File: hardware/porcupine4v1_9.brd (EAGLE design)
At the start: 24.4 x 27.4 mm, 33 parts, among them X1 PROGCON

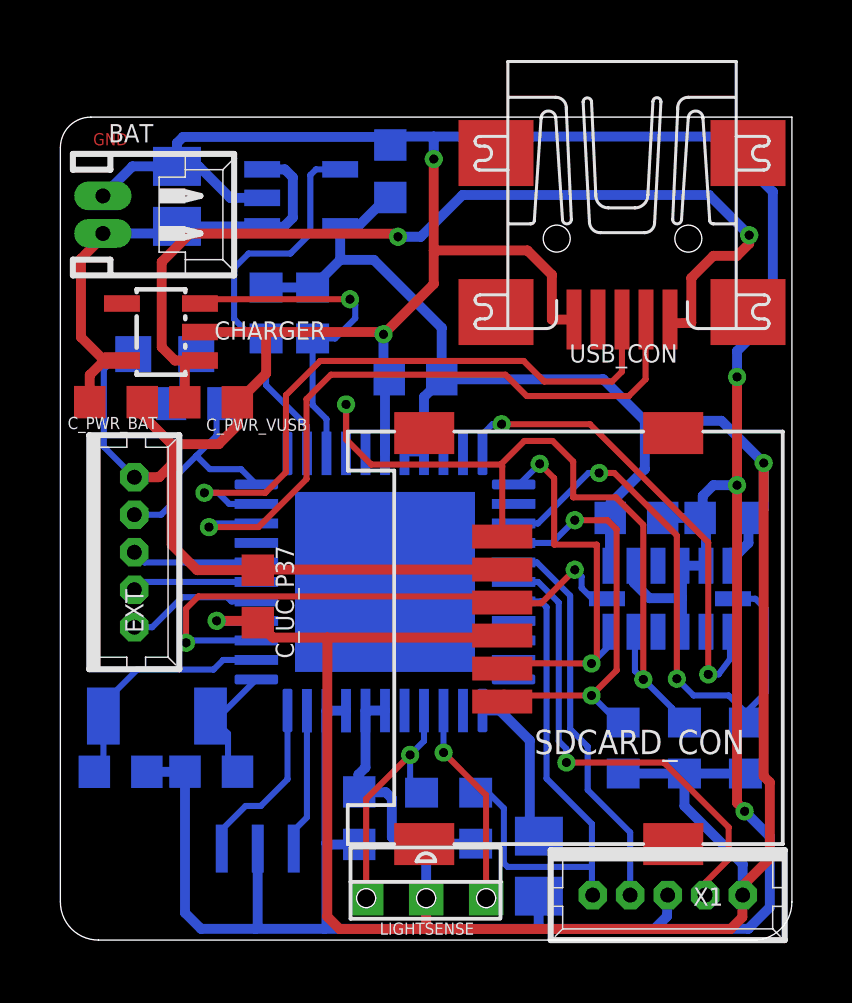
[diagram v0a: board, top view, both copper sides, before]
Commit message: updated porcupine4v1_9 for better placement of components; removed PWRGD
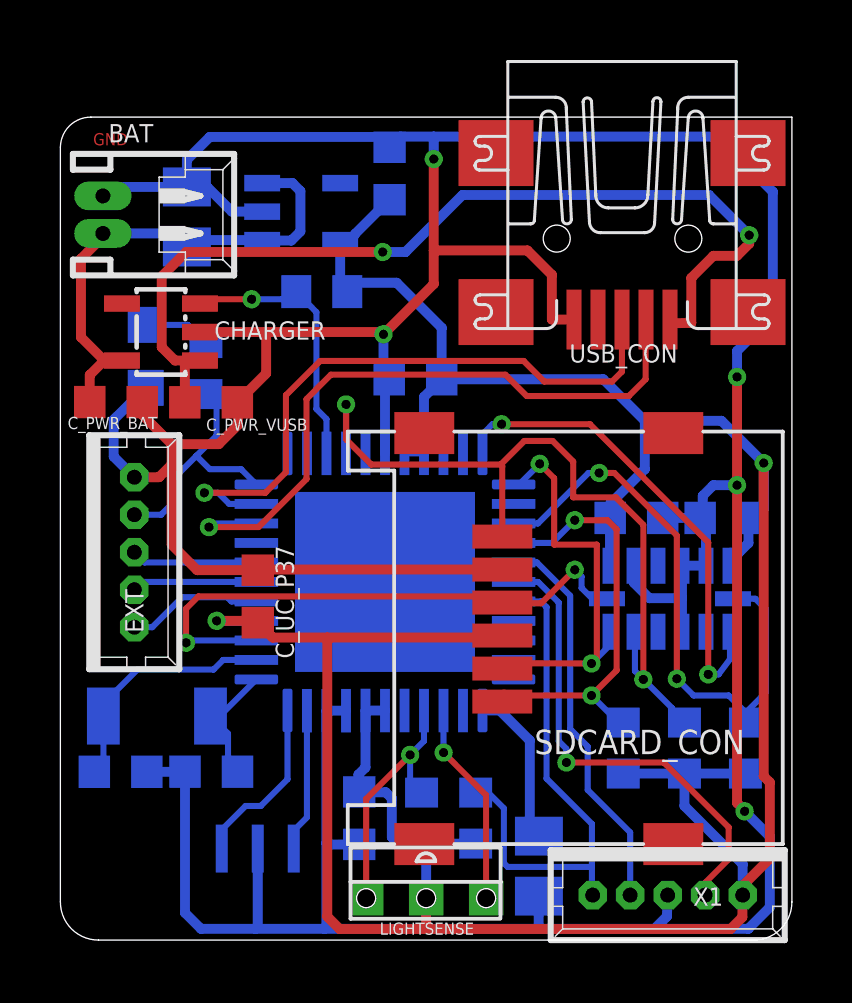
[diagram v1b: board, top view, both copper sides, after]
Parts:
- removed R7: 10k, rcl:R0603
- moved R8 1.21 mm to (4.85, 19.1), turned to 270 degrees
- moved R3 0.77 mm to (8.71, 21.6), turned to 180 degrees
- moved C_PWR_SW 0.76 mm to (4.22, 24.1)
- moved LED1 0.64 mm to (2.84, 19.5), turned to 90 degrees
- moved LDO 0.46 mm to (8.03, 24.3)
- moved C_PWR_VREG 0.08 mm to (11.0, 25.6)
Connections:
- removed net PWRGD: LDO.4, PIC_CONTROLLER.2, R7.1
- net +3V3: no longer R7.2
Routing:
- net PWRGD: track 13.5 -> 0.00 mm
- net GND: track 158.6 -> 155.9 mm
- net POK: track 11.5 -> 9.16 mm
- net +3V3: track 109.8 -> 107.5 mm

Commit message: updated basic 4.1.9
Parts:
- removed EXT: PROGCON, HedgehogLib:53047-05-OCT
- removed LED1: (no value), led:SML0805
- removed R8: 220, rcl:R0603
- moved C2_32KHZ 1.91 mm to (4.11, 3.94), turned to 270 degrees
- moved C1_32KHZ 1.73 mm to (2.46, 3.94), turned to 270 degrees
- moved C_PWR_VUSB 1.52 mm to (3.80, 17.0), turned to 270 degrees
- moved 32KHZ_CRYSTAL 1.15 mm to (3.99, 6.60)
- moved C_PWR_BAT 1.01 mm to (2.34, 17.0), turned to 270 degrees
- moved R6 0.74 mm to (22.1, 6.40)
- moved C_PWR_SW 0.51 mm to (3.99, 23.6)
- moved C_PWR_VREG 0.49 mm to (11.0, 25.1)
- moved R2 0.38 mm to (20.4, 6.40)
- moved 12MHZ_RESONATOR 0.28 mm to (6.83, 3.17), turned to 270 degrees
- moved C_UC_P37 0.08 mm to (6.66, 11.5)
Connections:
- removed net EXT1: EXT.1, PIC_CONTROLLER.38
- removed net EXT2: EXT.2, PIC_CONTROLLER.39
- removed net EXT3: EXT.3, PIC_CONTROLLER.40
- removed net EXT4: EXT.4, PIC_CONTROLLER.44, R8.2
- removed net N$4: LED1.A, R8.1
- net GND: no longer EXT.5, LED1.C
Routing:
- net GND: track 155.9 -> 144.5 mm
- net EXT4: track 8.24 -> 0.00 mm
- net EXT1: track 4.54 -> 0.00 mm
- net EXT3: track 4.21 -> 0.00 mm
- net EXT2: track 4.18 -> 0.00 mm
- net N$4: track 2.26 -> 0.00 mm
- net N$1: track 4.78 -> 6.80 mm
- net N$2: track 5.81 -> 3.87 mm
- net SCLK: track 19.0 -> 20.5 mm
- net N$3: track 4.26 -> 5.72 mm

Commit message: eagle design update basic 4.1.9
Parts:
- moved C1_32KHZ 4.02 mm to (1.95, 7.92)
- moved C2_32KHZ 2.39 mm to (1.93, 4.90), turned to 90 degrees
- moved 32KHZ_CRYSTAL 0.39 mm to (3.91, 6.99), turned to 90 degrees
- moved C_PWR_BAT 0.38 mm to (1.96, 17.0)
- moved 12MHZ_RESONATOR 0.36 mm to (6.48, 3.23), turned to 180 degrees
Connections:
- net V_USB: now also CHARGER.4
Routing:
- net GND: track 144.5 -> 152.7 mm
- net N$6: track 8.19 -> 4.80 mm
- net N$1: track 6.80 -> 4.61 mm
- net N$3: track 5.72 -> 7.70 mm
- net V_USB: track 31.8 -> 33.5 mm
- net N$2: track 3.87 -> 5.37 mm

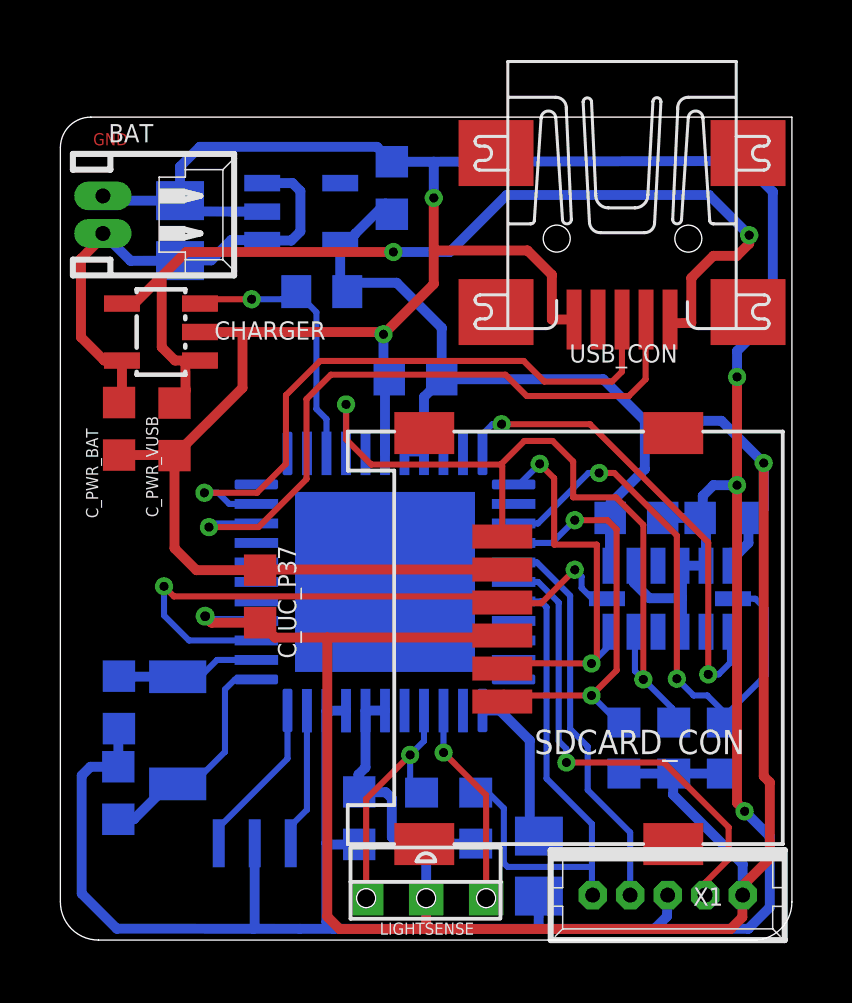
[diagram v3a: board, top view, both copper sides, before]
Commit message: hardware version 4v1_9 updated, removed c_pwr_sw capacitor
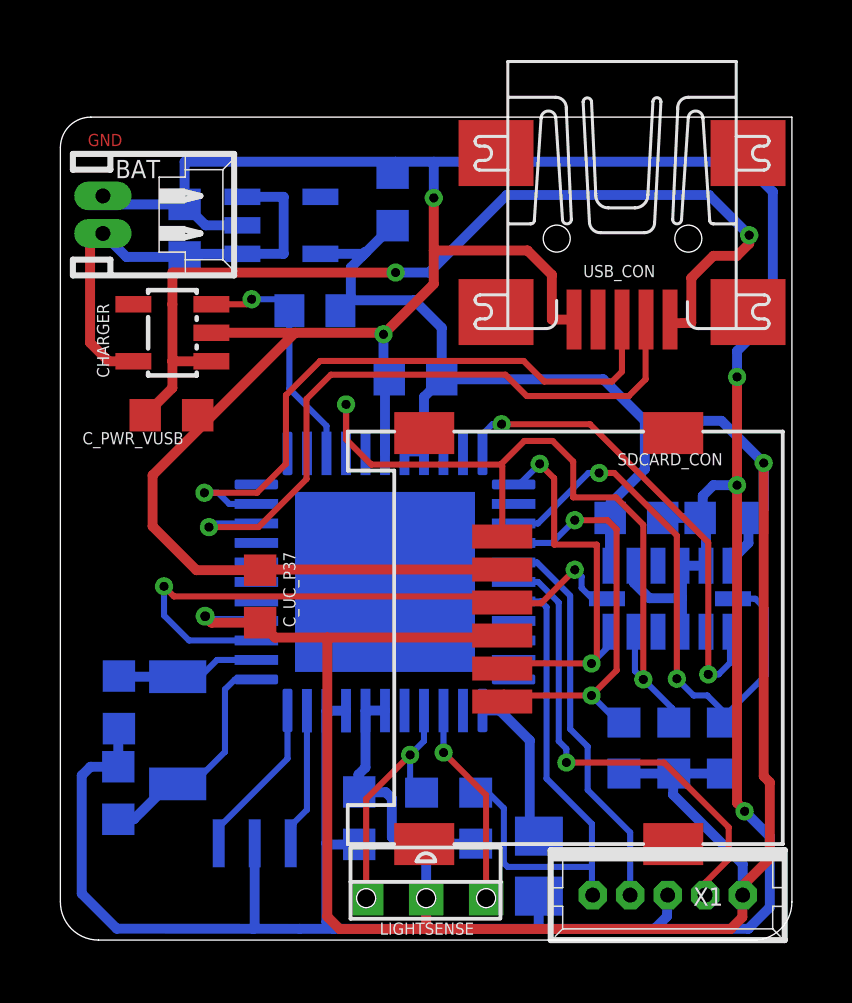
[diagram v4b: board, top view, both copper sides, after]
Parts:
- removed C_PWR_SW: 10u, rcl:C0805K
- C_PWR_BAT: value 1u -> 4.7u
- moved C_PWR_BAT 6.96 mm to (4.14, 23.6), flipped to the bottom, turned to 90 degrees
- moved LDO 0.80 mm to (7.37, 23.8)
- moved R3 0.67 mm to (8.48, 21.0)
- moved C_PWR_VUSB 0.48 mm to (3.70, 17.5), turned to 0 degrees
- moved CHARGER 0.38 mm to (3.73, 20.2)
- moved C_PWR_VREG 0.38 mm to (11.1, 24.7)
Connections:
- net GND: no longer C_PWR_SW.2
- net V_BAT: no longer C_PWR_SW.1
- net V_USB: no longer CHARGER.4
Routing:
- net V_BAT: track 17.0 -> 15.2 mm
- net GND: track 152.7 -> 151.6 mm
- net V_USB: track 33.5 -> 32.4 mm
- net POK: track 9.16 -> 8.21 mm

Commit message: version 4.1.9 pre-order
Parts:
- moved C_PWR_BAT 0.47 mm to (3.68, 23.7)
- moved BAT 0.18 mm to (2.67, 24.4)
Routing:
- net SDO: track 26.5 -> 28.0 mm
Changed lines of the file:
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@@
 <attribute name="VALUE" x="6.9088" y="18.3388" size="1.27" layer="27" rot="R90"/>
 </element>
-<element name="C_PWR_BAT" library="rcl" package="C0603K" value="4.7u" x="4.1402" y="23.6474" smashed="yes" rot="MR90">
-<attribute name="NAME" x="5.88" y="25.7706" size="0.4064" layer="26" rot="MR0"/>
-<attribute name="VALUE" x="2.4902" y="22.8474" size="1.016" layer="28" rot="MR90"/>
+<element name="C_PWR_BAT" library="rcl" package="C0603K" value="4.7u" x="3.683" y="23.749" smashed="yes" rot="MR90">
+<attribute name="NAME" x="5.4228" y="25.8722" size="0.4064" layer="26" rot="MR0"/>
+<attribute name="VALUE" x="2.033" y="22.949" size="1.016" layer="28" rot="MR90"/>
 </element>
 <element name="ACCELEROMETER" library="HedgehogLib" package="LGA14" value="ADXL345" x="20.32" y="11.3792" smashed="yes" rot="MR0">
@@
 <attribute name="FARNELL" value="2101349" x="3.9116" y="6.985" size="1.778" layer="28" rot="MR90" display="off"/>
 </element>
-<element name="BAT" library="con-molex" package="53048-02" value="53048-02" x="2.667" y="24.1808" smashed="yes" rot="R270">
-<attribute name="OC_NEWARK" value="57H4718" x="2.667" y="24.1808" size="1.778" layer="27" rot="R270" display="off"/>
-<attribute name="MPN" value="53048-0210" x="2.667" y="24.1808" size="1.778" layer="27" rot="R270" display="off"/>
-<attribute name="MF" value="MOLEX" x="2.667" y="24.1808" size="1.778" layer="27" rot="R270" display="off"/>
-<attribute name="OC_FARNELL" value="1012259" x="2.667" y="24.1808" size="1.778" layer="27" rot="R270" display="off"/>
-<attribute name="NAME" x="1.8334" y="25.3968" size="0.6096" layer="25"/>
-<attribute name="VALUE" x="-1.208" y="26.1808" size="1.27" layer="27" rot="R270"/>
+<element name="BAT" library="con-molex" package="53048-02" value="53048-02" x="2.667" y="24.3586" smashed="yes" rot="R270">
+<attribute name="OC_NEWARK" value="57H4718" x="2.667" y="24.3586" size="1.778" layer="27" rot="R270" display="off"/>
+<attribute name="MPN" value="53048-0210" x="2.667" y="24.3586" size="1.778" layer="27" rot="R270" display="off"/>
+<attribute name="MF" value="MOLEX" x="2.667" y="24.3586" size="1.778" layer="27" rot="R270" display="off"/>
+<attribute name="OC_FARNELL" value="1012259" x="2.667" y="24.3586" size="1.778" layer="27" rot="R270" display="off"/>
+<attribute name="NAME" x="1.8334" y="25.5746" size="0.6096" layer="25"/>
+<attribute name="VALUE" x="-1.208" y="26.3586" size="1.27" layer="27" rot="R270"/>
 </element>
 <element name="12MHZ_RESONATOR" library="HedgehogLib" package="PRQC-C" value="RESONATORPRQC-C" x="6.477" y="3.2258" rot="MR180">
@@
 <wire x1="1.8796" y1="0.381" x2="0.7112" y2="1.5494" width="0.3302" layer="16"/>
 <wire x1="0.7112" y1="1.5494" x2="0.7112" y2="5.4864" width="0.3302" layer="16"/>
-<wire x1="4.1402" y1="25.9448" x2="11.176" y2="25.9448" width="0.3302" layer="16"/>
+<wire x1="5.0038" y1="25.9448" x2="11.176" y2="25.9448" width="0.3302" layer="16"/>
 <wire x1="11.176" y1="25.9448" x2="12.446" y2="25.9448" width="0.3302" layer="16"/>
 <wire x1="11.0744" y1="25.5638" x2="11.0744" y2="25.8432" width="0.3302" layer="16"/>
 <wire x1="11.0744" y1="25.8432" x2="11.176" y2="25.9448" width="0.3302" layer="16"/>
-<wire x1="4.1402" y1="25.9448" x2="4.1402" y2="24.5224" width="0.3302" layer="16"/>
-<wire x1="4.1402" y1="24.5224" x2="1.921" y2="24.5224" width="0.3302" layer="16"/>
-<wire x1="1.921" y1="24.5224" x2="1.417" y2="24.8058" width="0.3302" layer="16"/>
+<wire x1="5.0038" y1="25.9448" x2="3.683" y2="24.624" width="0.3302" layer="16"/>
+<wire x1="3.683" y1="24.624" x2="3.3688" y2="24.9796" width="0.3302" layer="16"/>
+<wire x1="3.3688" y1="24.9796" x2="1.417" y2="24.9836" width="0.3302" layer="16"/>
 <wire x1="3.0734" y1="13.7922" x2="4.5352" y2="12.3304" width="0.3302" layer="1"/>
 <wire x1="3.0734" y1="13.7922" x2="3.0734" y2="15.494" width="0.3302" layer="1"/>
@@
 <wire x1="10.7188" y1="20.2438" x2="10.7696" y2="20.193" width="0.3302" layer="1"/>
 <contactref element="LDO" pad="2"/>
-<wire x1="6.0659" y1="23.8252" x2="4.8374" y2="23.8252" width="0.3302" layer="16"/>
-<wire x1="4.8374" y1="23.8252" x2="4.1402" y2="24.5224" width="0.3302" layer="16"/>
+<wire x1="6.0659" y1="23.8252" x2="5.1168" y2="23.8252" width="0.3302" layer="16"/>
+<wire x1="5.1168" y1="23.8252" x2="4.2926" y2="24.638" width="0.3302" layer="16"/>
+<wire x1="4.2926" y1="24.638" x2="4.0754" y2="24.8666" width="0.3302" layer="16"/>
+<wire x1="4.0754" y1="24.8666" x2="3.683" y2="24.624" width="0.3302" layer="16"/>
 </signal>
 <signal name="USB_D+@RC5">
@@
 <wire x1="6.6576" y1="10.5804" x2="7.1542" y2="10.0838" width="0.3302" layer="1"/>
 <wire x1="7.1542" y1="10.0838" x2="8.8968" y2="10.0838" width="0.3302" layer="1"/>
-<wire x1="10.1714" y1="22.9108" x2="11.0744" y2="23.8138" width="0.3302" layer="16"/>
+<wire x1="10.0641" y1="22.8035" x2="11.0744" y2="23.8138" width="0.3302" layer="16"/>
 <wire x1="9.6821" y1="22.4215" x2="9.6821" y2="21.3271" width="0.3302" layer="16"/>
-<wire x1="10.146" y1="22.9362" x2="10.1714" y2="22.9108" width="0.3302" layer="16"/>
-<wire x1="10.1714" y1="22.9108" x2="10.0641" y2="22.8035" width="0.3302" layer="16"/>
 <contactref element="LDO" pad="5"/>
 <wire x1="10.0641" y1="22.8035" x2="9.6821" y2="22.4215" width="0.3302" layer="16"/>
@@
 <wire x1="9.5204" y1="17.6322" x2="9.525" y2="17.8562" width="0.2032" layer="16"/>
 <via x="9.525" y="17.8562" extent="1-16" drill="0.3048" shape="octagon"/>
-<wire x1="9.525" y1="17.8562" x2="9.525" y2="16.6878" width="0.2032" layer="1"/>
-<wire x1="9.525" y1="16.6878" x2="10.36224375" y2="15.85055625" width="0.2032" layer="1"/>
-<wire x1="10.36224375" y1="15.85055625" x2="14.678796875" y2="15.85055625" width="0.2032" layer="1"/>
+<wire x1="9.525" y1="17.8562" x2="9.525" y2="16.4084" width="0.2032" layer="1"/>
+<wire x1="9.525" y1="16.4084" x2="10.36224375" y2="15.57115625" width="0.2032" layer="1"/>
+<wire x1="10.36224375" y1="15.57115625" x2="13.332596875" y2="15.57115625" width="0.2032" layer="1"/>
 <wire x1="19.1516" y1="10.3124" x2="19.1516" y2="8.9694" width="0.2032" layer="16"/>
 <wire x1="19.1516" y1="8.9694" x2="19.431" y2="8.69" width="0.2032" layer="16"/>
@@
 <wire x1="20.3962" y1="7.2898" x2="20.3962" y2="7.7248" width="0.2032" layer="16"/>
 <wire x1="20.3962" y1="7.7248" x2="19.431" y2="8.69" width="0.2032" layer="16"/>
-<wire x1="14.678796875" y1="15.85055625" x2="15.465240625" y2="16.637" width="0.2032" layer="1"/>
+<wire x1="13.332596875" y1="15.57115625" x2="14.4018" y2="15.5702" width="0.2032" layer="1"/>
+<wire x1="14.4018" y1="15.5702" x2="15.465240625" y2="16.633640625" width="0.2032" layer="1"/>
+<wire x1="15.465240625" y1="16.633640625" x2="15.465240625" y2="16.637" width="0.2032" layer="1"/>
 <wire x1="15.465240625" y1="16.637" x2="16.4084" y2="16.637" width="0.2032" layer="1"/>
-<wire x1="14.678796875" y1="15.85055625" x2="14.7292" y2="15.800153125" width="0.2032" layer="1"/>
-<wire x1="14.7292" y1="15.800153125" x2="14.7292" y2="13.4504" width="0.2032" layer="1"/>
+<wire x1="13.332596875" y1="15.57115625" x2="13.3322" y2="13.463353125" width="0.2032" layer="1"/>
+<wire x1="13.3322" y1="13.463353125" x2="14.7292" y2="13.4504" width="0.2032" layer="1"/>
 </signal>
 <signal name="CS_ADX">
@@
 <contactref element="C_PWR_BAT" pad="1"/>
 <contactref element="BAT" pad="1"/>
-<wire x1="1.417" y1="23.5558" x2="2.2004" y2="22.7724" width="0.3302" layer="16"/>
-<wire x1="2.2004" y1="22.7724" x2="4.1402" y2="22.7724" width="0.3302" layer="16"/>
+<wire x1="1.417" y1="23.7336" x2="2.2766" y2="22.874" width="0.3302" layer="16"/>
+<wire x1="2.2766" y1="22.874" x2="3.683" y2="22.874" width="0.3302" layer="16"/>
 <wire x1="2.4338" y1="19.2938" x2="1.6104" y2="19.2938" width="0.3302" layer="1"/>
 <wire x1="1.6104" y1="19.2938" x2="0.9906" y2="19.9136" width="0.3302" layer="1"/>
 <wire x1="0.9906" y1="19.9136" x2="0.9906" y2="23.1294" width="0.3302" layer="1"/>
-<wire x1="0.9906" y1="23.1294" x2="1.417" y2="23.5558" width="0.3302" layer="1"/>
+<wire x1="0.9906" y1="23.1294" x2="1.417" y2="23.7336" width="0.3302" layer="1"/>
 <contactref element="LDO" pad="1"/>
 <contactref element="LDO" pad="3"/>
@@
 <wire x1="7.4422" y1="22.8752" x2="7.4422" y2="24.7752" width="0.3302" layer="16"/>
 <wire x1="7.4422" y1="24.7752" x2="6.0659" y2="24.7752" width="0.3302" layer="16"/>
-<wire x1="4.1402" y1="22.7724" x2="4.6724" y2="22.8752" width="0.3302" layer="16"/>
+<wire x1="3.683" y1="22.874" x2="4.6724" y2="22.8752" width="0.3302" layer="16"/>
 <wire x1="4.6724" y1="22.8752" x2="6.0659" y2="22.8752" width="0.3302" layer="16"/>
 </signal>
